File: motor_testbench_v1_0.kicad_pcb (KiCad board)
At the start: 4 copper layers, 132.8 x 73 mm, 166 parts, among them J1 Conn_01x03_Pin, J10 V_bat_secondary, J11 Conn_01x02_Pin, J12 Conn_01x02_Pin, J2 Conn_01x18_Pin, J3 V_bat_in, J4 V_bat_out, J5 Conn_01x05_Pin, J6 Conn_01x05_Pin, J7 Conn_01x05_Pin, J8 Conn_01x04_Pin, J9 Conn_01x02_Pin, U1 ESP32-S3-DevKitC, U10 TPS7A20xxxDQN, U11 TPS7A20xxxDQN, U12 MCP1501-18xSN, U3 MCP6022, U4 ACPL-C87A, U5 TLV77333PDBVR, U6 TPS62933, U7 TLV77333PDBVR, U8 TPS62933, U9 TLV77333PDBVR

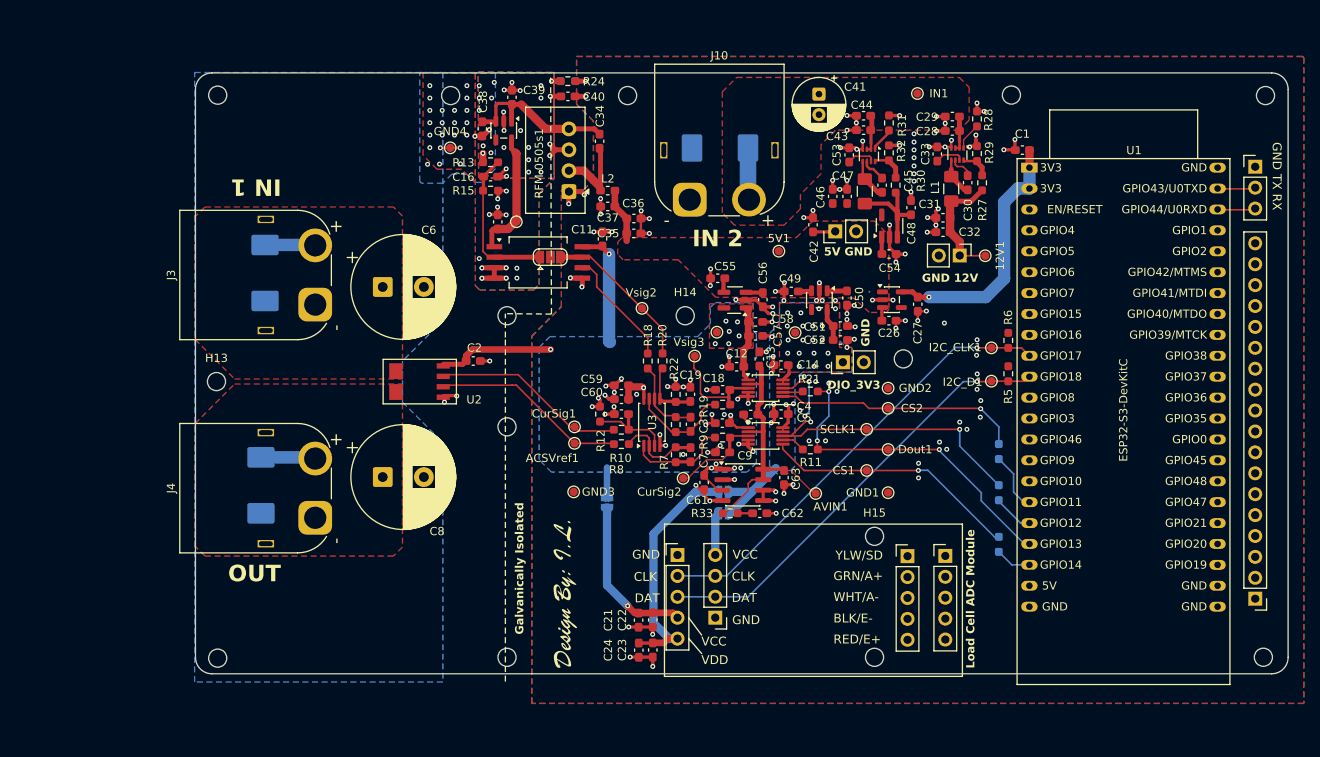
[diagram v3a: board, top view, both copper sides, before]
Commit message: Improved layout.
[KiCad Version: 9.0.8]
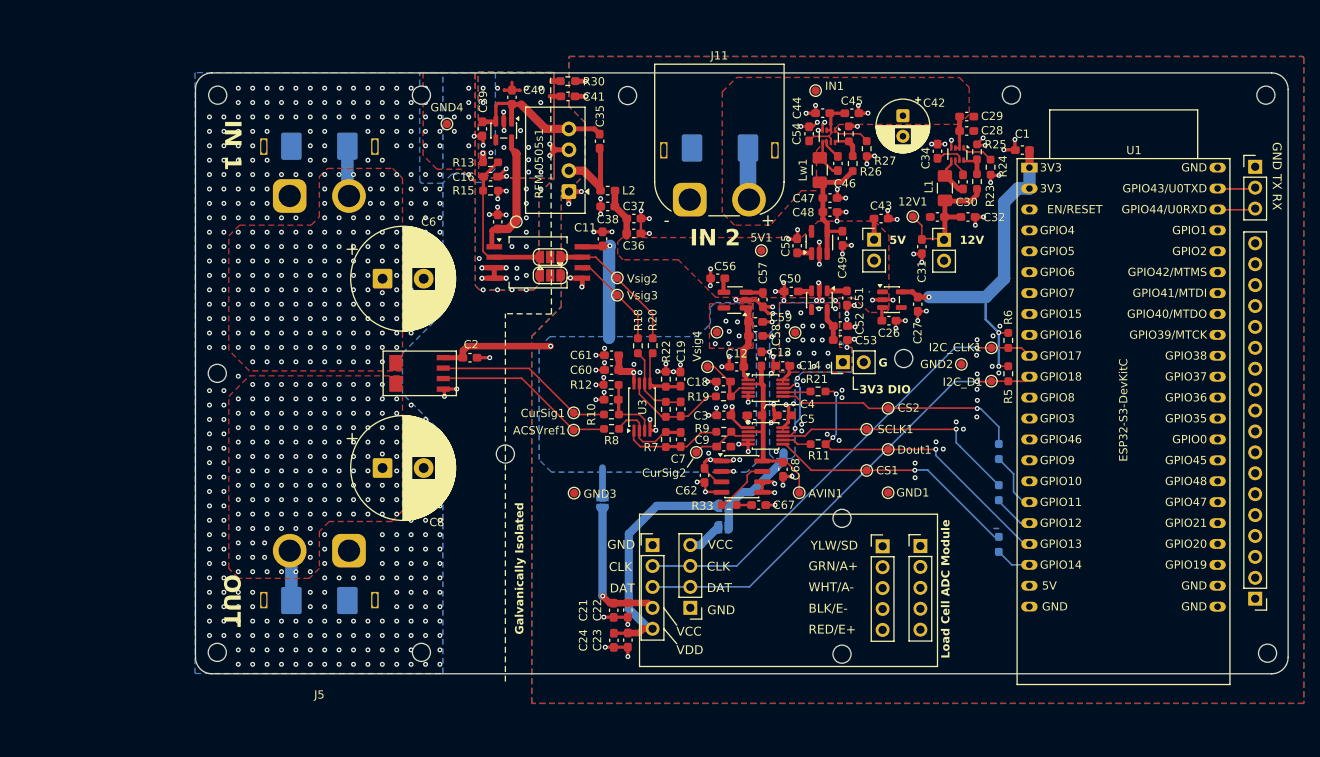
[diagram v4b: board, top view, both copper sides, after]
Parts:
- removed the C47 at (150.4, 54.5)
- removed G*** (x2): LOGO, LOGO
- removed H14: MountingHole, MountingHole:MountingHole_2.2mm_M2_DIN965
- removed the H4 at (109.1, 82.5)
- added C31: 1u, Capacitor_SMD:C_0603_1608Metric_Pad1.08x0.95mm_HandSolder, F.Cu at (159.5, 60.6)
- added C48: 22uF, Capacitor_SMD:C_0603_1608Metric_Pad1.08x0.95mm_HandSolder, F.Cu at (148.3, 56.4)
- added Vsig3: TestPoint, TestPoint:TestPoint_Pad_D1.0mm, F.Cu at (122.5, 66.5)
- JP5: moved to F.Cu
- moved H7 16.8 mm to (108.9, 85.8)
- moved D1 16.8 mm to (86.3, 48.4), turned to 0 degrees
- moved D2 15.7 mm to (86.3, 103.6), turned to 180 degrees
- moved J4 13.6 mm to (82.7, 54.5), turned to 0 degrees
- moved IN1 12.4 mm to (146.6, 41.6)
- moved C55 11.2 mm to (144.3, 60.5), turned to 90 degrees
- moved C42 10.5 mm to (157.2, 44.7)
- moved H11 10.4 mm to (98.7, 109.9)
- moved 12V1 10.0 mm to (158.4, 57.0), turned to 90 degrees
- moved GND2 9.36 mm to (164.3, 74.9)
- moved C49 9.13 mm to (149.8, 59.6), turned to -90 degrees
- moved U10 8.76 mm to (147.1, 60.1)
- moved C43 8.31 mm to (154.6, 57.2), turned to 0 degrees
- moved R24 6.09 mm to (167.8, 51.0), turned to -90 degrees
- moved Lw1 6.05 mm to (147.1, 51.3)
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- renumbered C31 to C32, C32 to C33, C33 to C34, C34 to C35, C35 to C36, C36 to C37, C37 to C38, C38 to C39, C39 to C40, C40 to C41, C41 to C42, C42 to C43, C43 to C44, C44 to C45, C45 to C46, C46 to C47, C48 to C49, C49 to C50, C50 to C51, C51 to C52, C52 to C53, C53 to C54, C54 to C55, C55 to C56, C56 to C57, C57 to C58, C58 to C59, C59 to C60, C60 to C61, C61 to C62, C62 to C67, C63 to C68, H11 to H10, H12 to H11, H13 to H12, H15 to H13, H5 to H4, H6 to H5, H7 to H6, H8 to H7, H9 to H8, H10 to H9, J9 to J10, J10 to J11, J11 to J12, J12 to J13, J3 to J4, J4 to J5, J5 to J6, J6 to J7, J7 to J8, J8 to J9, R27 to R23, R28 to R24, R29 to R25, R30 to R26, R31 to R27, R32 to R28, R23 to R29, R24 to R30, U12 to U13, Vsig3 to Vsig4
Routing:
- net ESP_3V3: track 31.8 -> 43.2 mm, vias 1 -> 3
- net GND: track 152.0 -> 144.6 mm, vias 152 -> 149
- net Net-(MCP2-AIN+): track 12.2 -> 7.98 mm
- net fan_out: track 14.6 -> 17.7 mm
- net Net-(U10-EN): track 12.3 -> 15.5 mm
- net Net-(MCP1-AIN+): track 10.7 -> 7.56 mm
- net Net-(J8-Pin_4): track 20.5 -> 17.4 mm
- net 1V8_MCP_AVIN: track 32.5 -> 29.6 mm
- net I2C_D: track 53.9 -> 56.6 mm
- net I2C_CLK: track 54.9 -> 57.5 mm
- net /Measurements/Vout_ref: track 14.9 -> 12.5 mm
- net SCLK: track 42.8 -> 40.5 mm
- net GND_ISO: track 33.1 -> 30.9 mm, vias 62 -> 362
- net Net-(U3A-+): track 10.5 -> 8.36 mm
- net /Measurements/V_sig: track 18.9 -> 16.9 mm
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- added copper zone on F.Cu, net /Measurements/V_bat_in
- added copper zone on In1.Cu, net /Measurements/V_bat_in
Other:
- board text added: "12V"
- board text added: "3V3 DIO"
- board text added: "5V"
- board text added: "G"
- board text removed: "5V GND"
- board text removed: "DIO_3V3"
- board text removed: "GND 12V"
